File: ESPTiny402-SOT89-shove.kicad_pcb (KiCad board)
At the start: 2 copper layers, 26.4 x 23.9 mm, 20 parts, among them J1 Conn_01x10_Male, J2 Conn_01x10_Male, J3 Conn_01x04_Male, U1 ESP-01v090, U2 ATtiny402-SS, U3 MCP1700

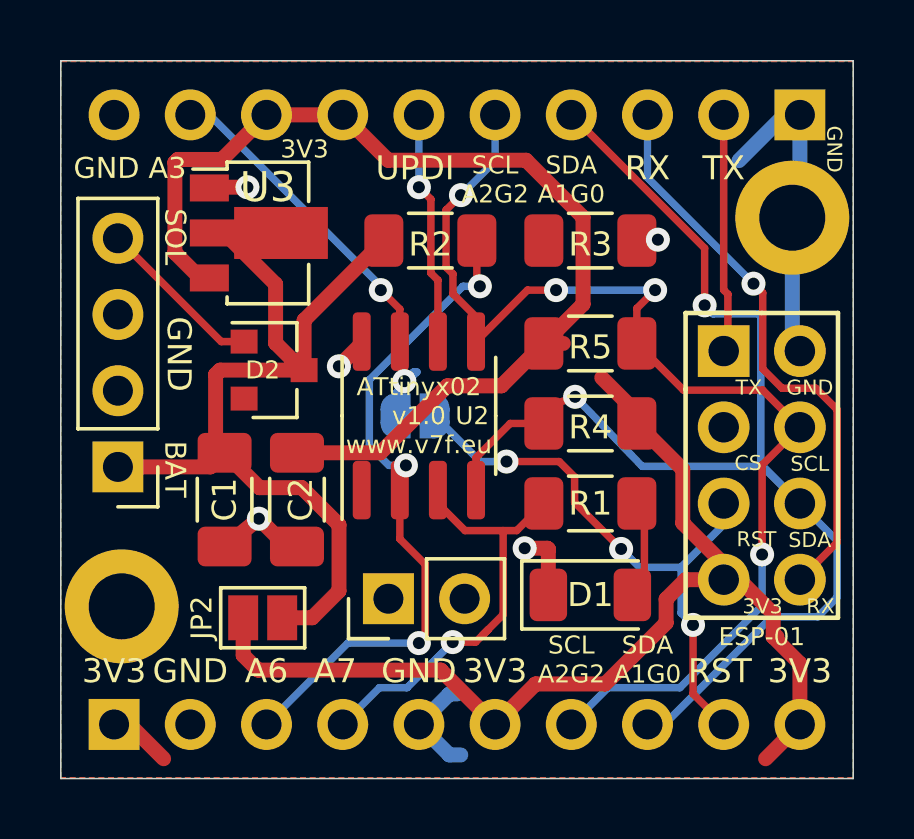
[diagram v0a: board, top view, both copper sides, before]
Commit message: Update for KiCad 9.0
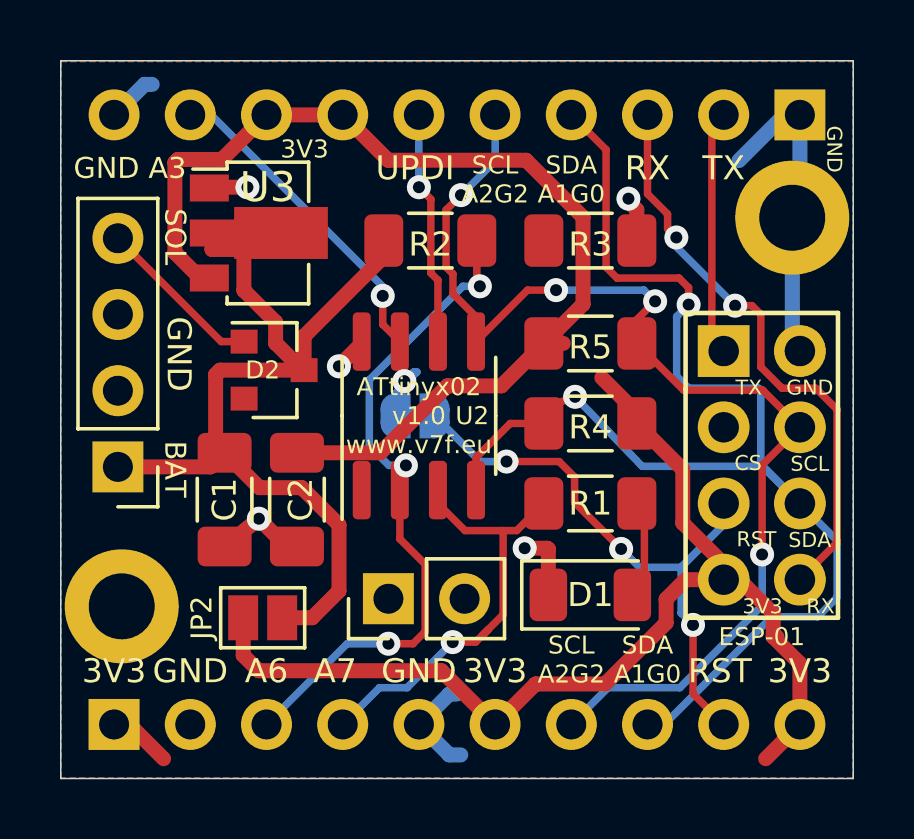
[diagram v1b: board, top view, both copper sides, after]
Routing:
- net GND: track 23.2 -> 26.1 mm
- net /SDA-A1: track 43.1 -> 45.2 mm
- net /RX: track 19.3 -> 19.6 mm, vias 1 -> 2

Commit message: Minor cosmetic cleanups
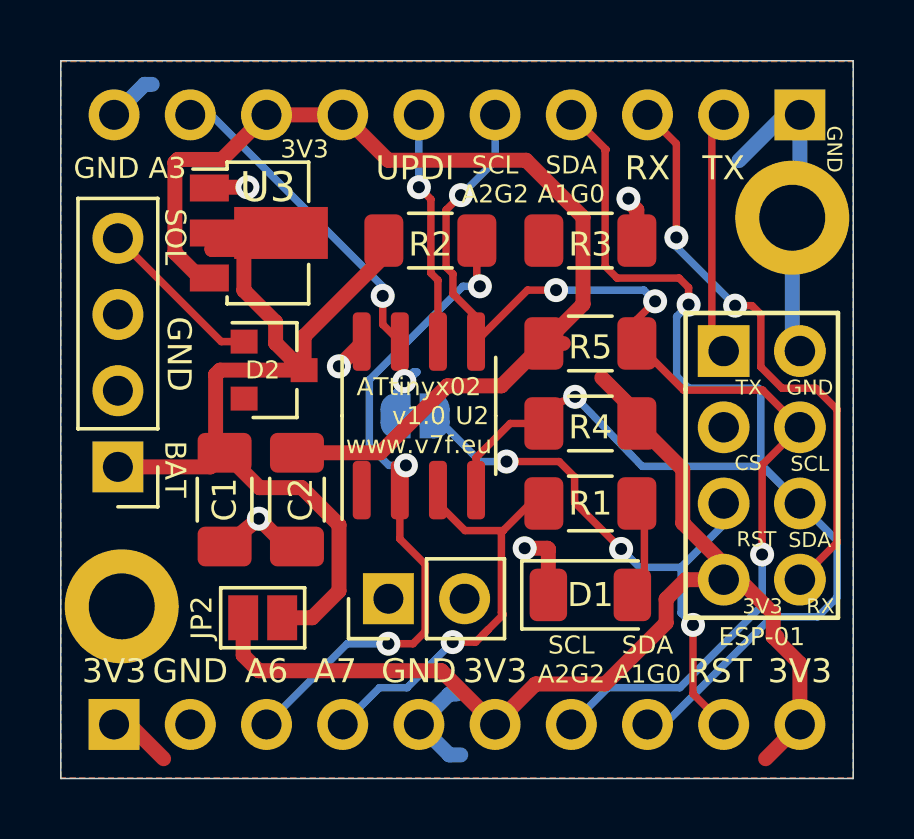
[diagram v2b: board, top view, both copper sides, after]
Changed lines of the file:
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@@
 		(0 "F.Cu" signal)
 		(2 "B.Cu" signal)
-		(9 "F.Adhes" user)
-		(11 "B.Adhes" user)
+		(9 "F.Adhes" user "F.Adhesive")
+		(11 "B.Adhes" user "B.Adhesive")
 		(13 "F.Paste" user)
 		(15 "B.Paste" user)
-		(5 "F.SilkS" user)
-		(7 "B.SilkS" user)
+		(5 "F.SilkS" user "F.Silkscreen")
+		(7 "B.SilkS" user "B.Silkscreen")
 		(1 "F.Mask" user)
 		(3 "B.Mask" user)
-		(17 "Dwgs.User" user)
-		(19 "Cmts.User" user)
-		(21 "Eco1.User" user)
-		(23 "Eco2.User" user)
+		(17 "Dwgs.User" user "User.Drawings")
+		(19 "Cmts.User" user "User.Comments")
+		(21 "Eco1.User" user "User.Eco1")
+		(23 "Eco2.User" user "User.Eco2")
 		(25 "Edge.Cuts" user)
 		(27 "Margin" user)
-		(31 "F.CrtYd" user)
-		(29 "B.CrtYd" user)
+		(31 "F.CrtYd" user "F.Courtyard")
+		(29 "B.CrtYd" user "B.Courtyard")
 		(35 "F.Fab" user)
 		(33 "B.Fab" user)
@@
 	)
 	(segment
+		(start 61.37102 55.118)
+		(end 61.823 55.118)
+		(width 0.25)
+		(layer "F.Cu")
+		(net 6)
+	)
+	(segment
 		(start 60.46701 56.02201)
 		(end 59.195532 56.02201)
@@
 	)
 	(segment
+		(start 60.46701 56.02201)
+		(end 61.37102 55.118)
+		(width 0.25)
+		(layer "F.Cu")
+		(net 6)
+	)
+	(segment
 		(start 59.770001 59.518001)
 		(end 59.961501 59.326501)
@@
 	)
 	(segment
-		(start 61.823 55.118)
-		(end 60.91899 56.02201)
+		(start 58.785225 59.739574)
+		(end 59.548428 59.739574)
 		(width 0.25)
 		(layer "F.Cu")
@@
 	)
 	(segment
-		(start 60.91899 56.02201)
+		(start 60.40752 56.0815)
 		(end 60.46701 56.02201)
 		(width 0.25)
@@
 	)
 	(segment
-		(start 60.46701 58.820992)
-		(end 60.46701 56.02201)
+		(start 59.548428 59.739574)
+		(end 59.961501 59.326501)
 		(width 0.25)
 		(layer "F.Cu")
@@
 	)
 	(segment
-		(start 58.785225 59.739574)
-		(end 59.548428 59.739574)
+		(start 60.40752 58.761502)
+		(end 60.40752 56.0815)
 		(width 0.25)
 		(layer "F.Cu")
@@
 	)
 	(segment
-		(start 59.548428 59.739574)
-		(end 59.961501 59.326501)
+		(start 60.46701 58.820992)
+		(end 60.40752 58.761502)
 		(width 0.25)
 		(layer "F.Cu")
@@
 	)
 	(segment
-		(start 65.94801 45.47111)
-		(end 65.94801 45.959904)
-		(width 0.25)
-		(layer "F.Cu")
-		(net 9)
-	)
-	(segment
 		(start 71.596601 51.983471)
 		(end 70.889731 51.276601)
@@
 	)
 	(segment
-		(start 65.278 42.164)
-		(end 65.278 44.8011)
-		(width 0.25)
-		(layer "F.Cu")
-		(net 9)
-	)
-	(segment
-		(start 65.94801 45.959904)
-		(end 66.239652 46.251546)
+		(start 69.056601 50.569731)
+		(end 69.056601 48.816304)
 		(width 0.25)
 		(layer "F.Cu")
@@
 	)
 	(segment
-		(start 65.278 44.8011)
-		(end 65.94801 45.47111)
+		(start 70.889731 51.276601)
+		(end 69.763471 51.276601)
 		(width 0.25)
 		(layer "F.Cu")
@@
 	)
 	(segment
-		(start 69.056601 50.569731)
-		(end 69.056601 48.816304)
+		(start 65.278 42.164)
+		(end 66.239652 43.125652)
 		(width 0.25)
 		(layer "F.Cu")
@@
 	)
 	(segment
-		(start 70.889731 51.276601)
-		(end 69.763471 51.276601)
+		(start 69.763471 51.276601)
+		(end 69.056601 50.569731)
 		(width 0.25)
 		(layer "F.Cu")
@@
 	)
 	(segment
-		(start 69.763471 51.276601)
-		(end 69.056601 50.569731)
+		(start 71.596601 56.419399)
+		(end 71.596601 51.983471)
 		(width 0.25)
 		(layer "F.Cu")
@@
 	)
 	(segment
-		(start 71.596601 56.419399)
-		(end 71.596601 51.983471)
+		(start 66.239652 43.125652)
+		(end 66.239652 46.251546)
 		(width 0.25)
 		(layer "F.Cu")
@@
 	)
 	(segment
-		(start 63.89799 43.32399)
-		(end 63.89799 47.23889)
+		(start 63.867 47.2079)
+		(end 64.26411 47.60501)
 		(width 0.25)
 		(layer "F.Cu")
@@
 	)
 	(segment
-		(start 66.330618 47.60501)
-		(end 66.648989 47.923381)
+		(start 64.26411 47.60501)
+		(end 66.330618 47.60501)
 		(width 0.25)
 		(layer "F.Cu")
@@
 	)
 	(segment
-		(start 63.89799 47.23889)
-		(end 64.26411 47.60501)
+		(start 61.823 51.934737)
+		(end 61.823 52.451)
 		(width 0.25)
 		(layer "F.Cu")
@@
 	)
 	(segment
-		(start 61.823 51.934737)
+		(start 60.701996 52.451)
 		(end 61.823 52.451)
 		(width 0.25)
@@
 	)
 	(segment
-		(start 60.701996 52.451)
-		(end 61.823 52.451)
+		(start 66.648989 47.923381)
+		(end 66.648989 48.489066)
 		(width 0.25)
 		(layer "F.Cu")
@@
 	)
 	(segment
-		(start 64.26411 47.60501)
-		(end 66.330618 47.60501)
+		(start 63.867 43.35498)
+		(end 63.867 47.2079)
 		(width 0.25)
 		(layer "F.Cu")
@@
 	)
 	(segment
-		(start 66.648989 47.923381)
-		(end 66.648989 48.489066)
+		(start 59.563 53.589996)
+		(end 60.701996 52.451)
 		(width 0.25)
 		(layer "F.Cu")
@@
 	)
 	(segment
-		(start 62.738 42.164)
-		(end 63.89799 43.32399)
+		(start 63.89799 43.32399)
+		(end 63.867 43.35498)
 		(width 0.25)
 		(layer "F.Cu")
@@
 	)
 	(segment
-		(start 59.563 53.589996)
-		(end 60.701996 52.451)
+		(start 62.738 42.164)
+		(end 63.89799 43.32399)
 		(width 0.25)
 		(layer "F.Cu")
@@
 		(width 0.25)
 		(layer "F.Cu")
+		(net 13)
+	)
+	(segment
+		(start 66.330618 47.60501)
+		(end 66.648989 47.923381)
+		(width 0.25)
+		(layer "F.Cu")
